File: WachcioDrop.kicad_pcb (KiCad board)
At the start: 4 copper layers, 267 x 100.5 mm, 70 parts, among them J1 Conn_02x20_Top_Bottom, J2 Conn_01x04, J3 Conn_01x03, J4 Screw_Terminal_01x02, J5 Conn_01x10_Socket, J6 Conn_02x20_Top_Bottom, K1 G3MB-202P, K2 G3MB-202P, K3 G3MB-202P, K4 G3MB-202P, K5 G3MB-202P, K6 G3MB-202P, K7 G3MB-202P, K8 G3MB-202P, K9 G3MB-202P, U1 TC00500 RTC DS3231, U2 ESP32-S3-DEVKITC-1-N8R2, U3 ULN2803A, U4 74HC595D_118, U5 ULN2803A, U6 74HC595D_118, U7 LM1117RS-3.3

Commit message: Almoust done
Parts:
- added J4: Conn_01x03, Connector_PinHeader_2.54mm:PinHeader_1x03_P2.54mm_Vertical, F.Cu at (274.5, 72.5)
- added REF**: MountingHole_3.5mm, MountingHole:MountingHole_3.5mm, F.Cu at (270.0, 27.0)
- added REF**: MountingHole_3.5mm, MountingHole:MountingHole_3.5mm, F.Cu at (244.0, 108.5)
- added REF**: MountingHole_3.5mm, MountingHole:MountingHole_3.5mm, F.Cu at (185.5, 19.0)
- D1: value ABS10 -> ABS10-DIODEC
- moved C3 11.7 mm to (253.5, 89.0), turned to -90 degrees
- moved PS1 8.75 mm to (254.0, 98.8)
- moved C7 5.59 mm to (257.6, 86.0)
- moved D1 5.32 mm to (271.0, 95.5), turned to 0 degrees
- moved C4 2.31 mm to (249.5, 80.0), turned to 90 degrees
- moved J3 2.00 mm to (278.5, 72.5)
- renumbered J4 to J5, J5 to J6, J6 to J7, R15 to R14, R16 to R15, R17 to R16, U7 to U3, U3 to U4, U4 to U5, U5 to U6, U6 to U7
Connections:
- D1 pad 3: Net-(D1-Pad3) -> /Główny/Shift_registers/AC_common
- J6 pad 10: /Główny/Shift_registers/AC_common_N -> /Główny/AC_common_N
- R10 pad 2: /Główny/Shift_registers/section4_LED_A -> /Główny/section4_LED_A
- R11 pad 2: /Główny/Shift_registers/section5_LED_A -> /Główny/section5_LED_A
- R12 pad 2: /Główny/Shift_registers/section6_LED_A -> /Główny/section6_LED_A
- R13 pad 2: /Główny/Shift_registers/section7_LED_A -> /Główny/section7_LED_A
- R14 pad 2: /Główny/Shift_registers/section8_LED_A -> /Główny/section8_LED_A
- R2 pad 2: Net-(D1-Pad3) -> /Główny/Shift_registers/AC_common
- R5 pad 2: /Główny/Shift_registers/zaw_g_LED_A -> /Główny/zaw_g_LED_A
- R6 pad 2: /Główny/Shift_registers/section1_LED_A -> /Główny/section1_LED_A
- R7 pad 2: /Główny/Shift_registers/section2_LED_A -> /Główny/section2_LED_A
- R9 pad 2: /Główny/Shift_registers/section3_LED_A -> /Główny/section3_LED_A
- U4 pad 1: /Główny/Shift_registers/zaw_g_LED_K -> /Główny/zaw_g_LED_K
- U4 pad 2: /Główny/Shift_registers/section1_LED_K -> /Główny/section1_LED_K
- U4 pad 3: /Główny/Shift_registers/section2_LED_K -> /Główny/section2_LED_K
- U4 pad 4: /Główny/Shift_registers/section3_LED_K -> /Główny/section3_LED_K
- U4 pad 5: /Główny/Shift_registers/section4_LED_K -> /Główny/section4_LED_K
- U4 pad 6: /Główny/Shift_registers/section5_LED_K -> /Główny/section5_LED_K
- U4 pad 7: /Główny/Shift_registers/section6_LED_K -> /Główny/section6_LED_K
- U4 pad 8: /Główny/Shift_registers/section7_LED_K -> /Główny/section7_LED_K
- U7 pad 1: /Główny/Shift_registers/wifi_status -> /Główny/wifi_status
- U7 pad 2: /Główny/Shift_registers/power_status -> /Główny/power_status
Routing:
- net /Główny/PIN_BTN_BACK: track 0.00 -> 70.6 mm, vias 0 -> 2
- net (no net): track 61.3 -> 0.00 mm
- net /Główny/AC_common_N: track 0.00 -> 59.9 mm
- net GND: track 88.8 -> 55.6 mm, vias 18 -> 13
- net +3.3V: track 52.9 -> 41.4 mm, vias 16 -> 10
- net +5V: track 153.9 -> 142.6 mm, vias 0 -> 1
- net /Główny/PIN_OLED_RESET: track 101.7 -> 94.1 mm
- net Net-(D1-+): track 19.4 -> 13.4 mm
- net /Główny/Shift_registers/AC_common: track 103.4 -> 108.9 mm, vias 0 -> 1
- net /Główny/PIN_OLED_CS: track 104.5 -> 101.2 mm
- net /Główny/zaw_g_LED_K: track 17.9 -> 15.0 mm
- net /Główny/PIN_DS18B20: track 90.1 -> 92.1 mm
- net /Główny/PIN_BTN_UP: track 26.1 -> 27.4 mm
- net /Główny/PIN_OLED_MOSI: track 77.7 -> 76.6 mm
- net /Główny/PIN_BTN_SELECT: track 30.3 -> 31.1 mm
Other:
- board text added: "1-wire"
- board text added: "24VAC"
- board text added: "3.3V"
- board text added: "3.3V status"
- board text added: "5V status"
- board text added: "800uF 50V"
- board text added: "Back"
- board text added: "Data"
- board text added: "Down"
- board text added: "GND"
- board text added: "I2C"
- board text added: "LED"
- board text added: "Power status"
- board text added: "SCL"
- board text added: "SDA"
- board text added: "SOIC127"
- board text added: "SOP18"
- board text added: "Section 1"
- board text added: "Section 2"
- board text added: "Section 3"
- board text added: "Section 4"
- board text added: "Section 5"
- board text added: "Section 6"
- board text added: "Section 7"
- board text added: "Section 8"
- board text added: "Section connection 1,2,3,4,5,6,7,8,main valve,common"
- board text added: "Select"
- board text added: "UP"
- board text added: "WachcioDrop v1.0 Wachcio 2026"
- board text added: "WiFi status"
- board text added: "main valve"

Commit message: Fix errors and and 3D models
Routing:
- net /Główny/PIN_OLED_CLK: track 0.00 -> 73.2 mm, vias 0 -> 4
- net /Główny/PIN_DS18B20: track 92.1 -> 91.2 mm

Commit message: genetare gerbers file
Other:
- board text added: "1"
- board text added: "2"
- board text added: "39"
- board text added: "40"
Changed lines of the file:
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@@
+		)
+	)
+	(gr_text "2"
+		(at 94.5 60.5 0)
+		(layer "B.SilkS")
+		(effects
+			(font
+				(size 1.5 1.5)
+				(thickness 0.3)
+				(bold yes)
+			)
+			(justify left bottom mirror)
+		)
+	)
+	(gr_text "40"
+		(at 94.5 108.5 0)
+		(layer "B.SilkS")
+		(effects
+			(font
+				(size 1.5 1.5)
+				(thickness 0.3)
+				(bold yes)
+			)
+			(justify left bottom mirror)
+		)
+	)
+	(gr_text "1"
+		(at 107.5 60.5 0)
+		(layer "B.SilkS")
+		(effects
+			(font
+				(size 1.5 1.5)
+				(thickness 0.3)
+				(bold yes)
+			)
+			(justify left bottom mirror)
+		)
+	)
+	(gr_text "39"
+		(at 107.5 108.5 0)
+		(layer "B.SilkS")
+		(effects
+			(font
+				(size 1.5 1.5)
+				(thickness 0.3)
+				(bold yes)
+			)
+			(justify left bottom mirror)
 		)
 	)

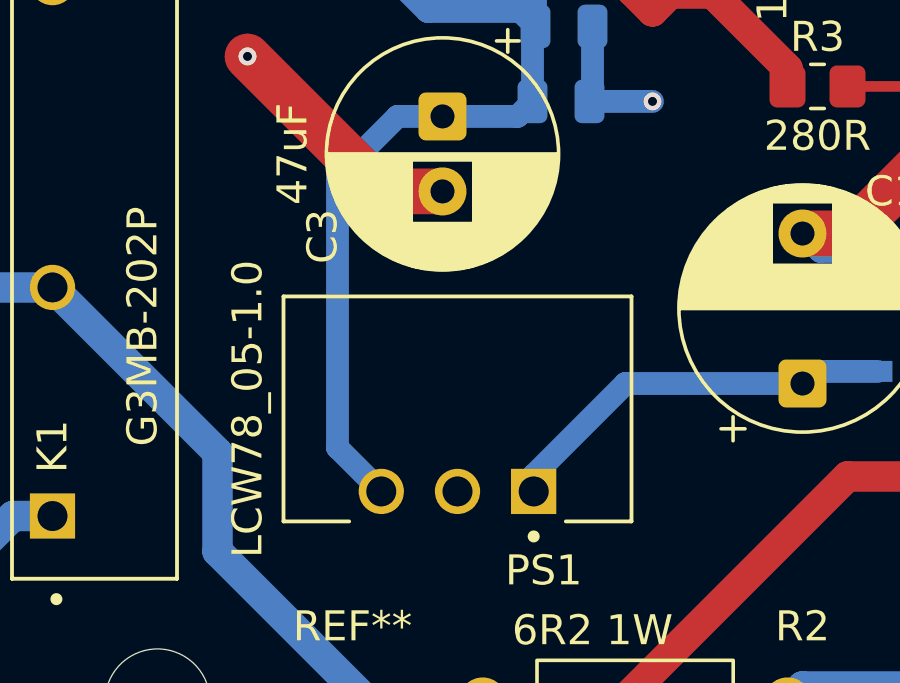
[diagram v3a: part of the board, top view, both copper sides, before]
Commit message: Add GND in PS1. Flip PS1
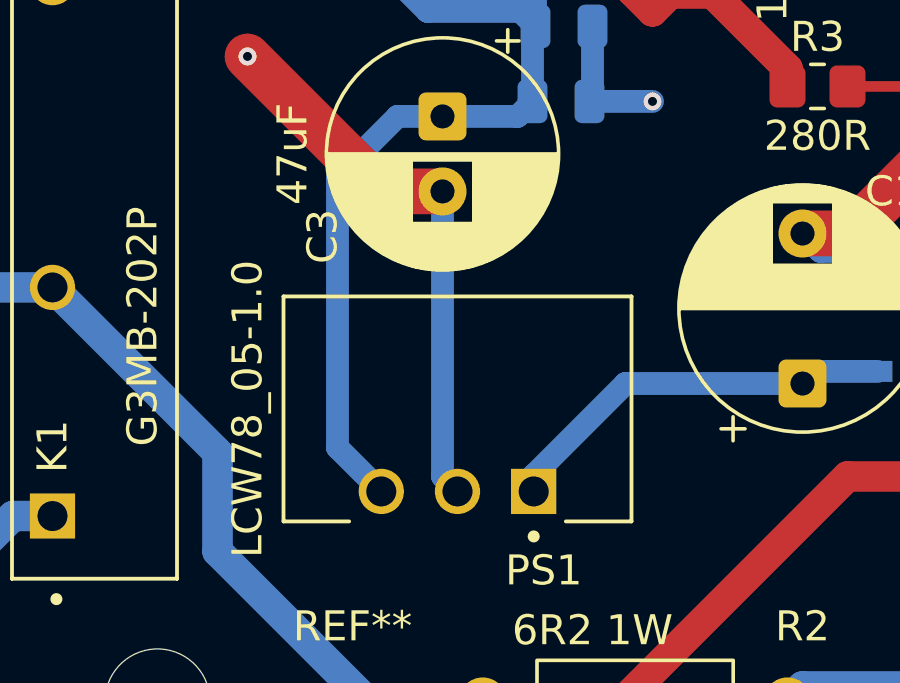
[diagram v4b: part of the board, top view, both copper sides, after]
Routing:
- net GND: track 55.6 -> 65.8 mm
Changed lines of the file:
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@@
+	)
+	(segment
+		(start 253.5 91.5)
+		(end 253.5 101)
+		(width 0.762)
+		(layer "B.Cu")
+		(net "GND")
 	)
 	(segment
@@
 		(width 0.762)
 		(layer "B.Cu")
+		(net "GND")
+	)
+	(segment
+		(start 253.5 101)
+		(end 254 101.5)
+		(width 0.762)
+		(layer "B.Cu")
